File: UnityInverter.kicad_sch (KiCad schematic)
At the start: 5 parts, among them U9 LM358

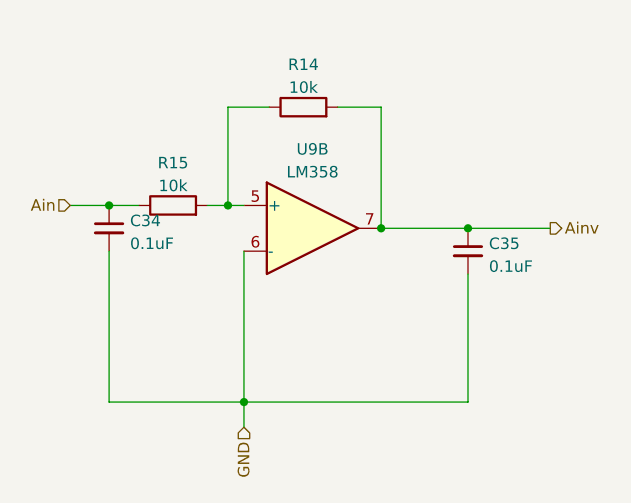
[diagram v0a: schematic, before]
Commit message: all SMD components going into boards
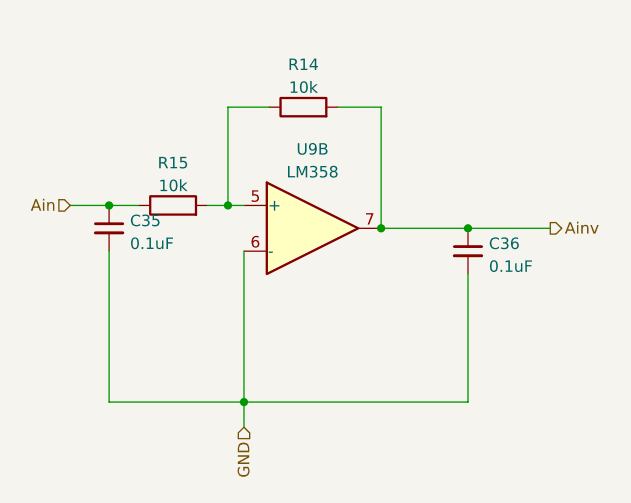
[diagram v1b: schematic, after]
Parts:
- U9: footprint (none) -> Package_TO_SOT_SMD:SOT-223-8
- renumbered C34 to C35, C35 to C36
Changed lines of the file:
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@@
   (symbol (lib_id "Device:C_Small") (at 112.776 105.156 0) (unit 1)
     (in_bom yes) (on_board yes) (fields_autoplaced)
-    (property "Reference" "C34" (id 0) (at 115.1001 104.3276 0)
+    (property "Reference" "C35" (id 0) (at 115.1001 104.3276 0)
       (effects (font (size 1.27 1.27)) (justify left))
     )
@@
     (property "Reference" "U9" (id 0) (at 135.382 96.3762 0))
     (property "Value" "LM358" (id 1) (at 135.382 98.9131 0))
-    (property "Footprint" "" (id 2) (at 135.382 105.156 0)
+    (property "Footprint" "Package_TO_SOT_SMD:SOT-223-8" (id 2) (at 135.382 105.156 0)
       (effects (font (size 1.27 1.27)) hide)
     )
@@
   (symbol (lib_id "Device:C_Small") (at 152.654 107.696 0) (unit 1)
     (in_bom yes) (on_board yes) (fields_autoplaced)
-    (property "Reference" "C35" (id 0) (at 154.9781 106.8676 0)
+    (property "Reference" "C36" (id 0) (at 154.9781 106.8676 0)
       (effects (font (size 1.27 1.27)) (justify left))
     )

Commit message: new board with SMD
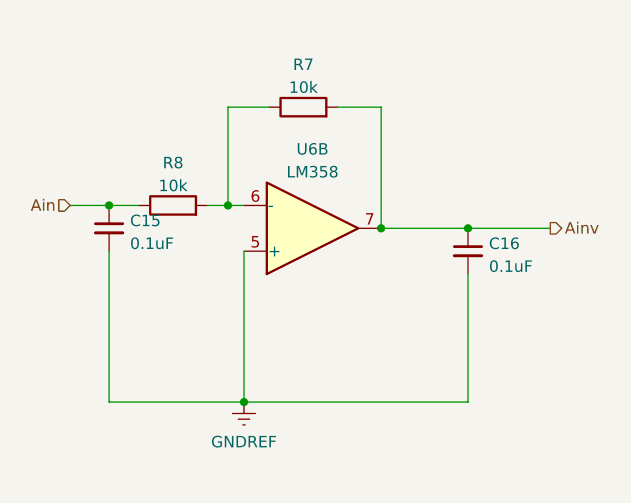
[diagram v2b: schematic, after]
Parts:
- renumbered C35 to C15, C36 to C16, R14 to R7, R15 to R8, U9 to U6
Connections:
- net at R7.1, R8.2: now also U6.6 (-); no longer U6.5 (+)
- net GND renamed GNDREF
- net GNDREF: now also U6.5 (+); no longer U6.6 (-)
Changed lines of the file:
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@@
-    (stroke (width 0) (type default) (color 0 0 0 0))
-  )
-  (wire (pts (xy 127.762 124.46) (xy 127.762 127.254))
     (stroke (width 0) (type default) (color 0 0 0 0))
   )
@@
     (effects (font (size 1.27 1.27)) (justify left))
   )
-  (hierarchical_label "GND" (shape input) (at 127.762 127.254 270)
-    (effects (font (size 1.27 1.27)) (justify right))
-  )
   (symbol (lib_id "Device:C_Small") (at 112.776 105.156 0) (unit 1)
     (in_bom yes) (on_board yes) (fields_autoplaced)
-    (property "Reference" "C35" (id 0) (at 115.1001 104.3276 0)
+    (property "Reference" "C15" (id 0) (at 115.1001 104.3276 0)
       (effects (font (size 1.27 1.27)) (justify left))
     )
@@
     (pin "2")
   )
-  (symbol (lib_id "Amplifier_Operational:LM358") (at 135.382 105.156 0) (unit 2)
+  (symbol (lib_id "Amplifier_Operational:LM358") (at 135.382 105.156 0) (mirror x) (unit 2)
     (in_bom yes) (on_board yes) (fields_autoplaced)
-    (property "Reference" "U9" (id 0) (at 135.382 96.3762 0))
+    (property "Reference" "U6" (id 0) (at 135.382 96.3762 0))
     (property "Value" "LM358" (id 1) (at 135.382 98.9131 0))
     (property "Footprint" "Package_TO_SOT_SMD:SOT-223-8" (id 2) (at 135.382 105.156 0)
@@
   (symbol (lib_id "Device:C_Small") (at 152.654 107.696 0) (unit 1)
     (in_bom yes) (on_board yes) (fields_autoplaced)
-    (property "Reference" "C36" (id 0) (at 154.9781 106.8676 0)
+    (property "Reference" "C16" (id 0) (at 154.9781 106.8676 0)
       (effects (font (size 1.27 1.27)) (justify left))
     )
@@
   (symbol (lib_id "Device:R") (at 119.888 102.616 90) (unit 1)
     (in_bom yes) (on_board yes) (fields_autoplaced)
-    (property "Reference" "R15" (id 0) (at 119.888 97.9002 90))
+    (property "Reference" "R8" (id 0) (at 119.888 97.9002 90))
     (property "Value" "10k" (id 1) (at 119.888 100.4371 90))
     (property "Footprint" "Resistor_SMD:R_0603_1608Metric" (id 2) (at 119.888 104.394 90)
@@
   (symbol (lib_id "Device:R") (at 134.366 91.694 90) (unit 1)
     (in_bom yes) (on_board yes) (fields_autoplaced)
-    (property "Reference" "R14" (id 0) (at 134.366 86.9782 90))
+    (property "Reference" "R7" (id 0) (at 134.366 86.9782 90))
     (property "Value" "10k" (id 1) (at 134.366 89.5151 90))
     (property "Footprint" "Resistor_SMD:R_0603_1608Metric" (id 2) (at 134.366 93.472 90)
@@
     (pin "2")
   )
+  (symbol (lib_id "power:GNDREF") (at 127.762 124.46 0) (unit 1)
+    (in_bom yes) (on_board yes) (fields_autoplaced)
+    (property "Reference" "#PWR017" (id 0) (at 127.762 130.81 0)
+      (effects (font (size 1.27 1.27)) hide)
+    )
+    (property "Value" "GNDREF" (id 1) (at 127.762 128.9034 0))
+    (property "Footprint" "" (id 2) (at 127.762 124.46 0)
+      (effects (font (size 1.27 1.27)) hide)
+    )
+    (property "Datasheet" "" (id 3) (at 127.762 124.46 0)
+      (effects (font (size 1.27 1.27)) hide)
+    )
+    (pin "1")
+  )
 )

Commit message: New single board with all SMD in progress
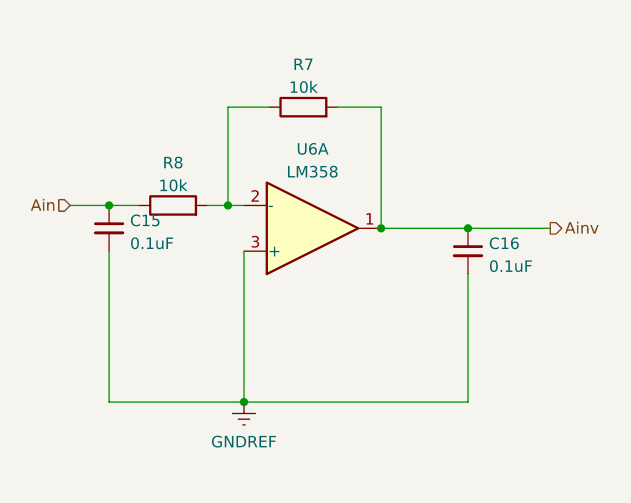
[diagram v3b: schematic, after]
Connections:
- net Ainv: now also U6.1; no longer U6.7
- net GNDREF: now also U6.3 (+); no longer U6.5 (+)
- net at R7.1, R8.2: now also U6.2 (-); no longer U6.6 (-)
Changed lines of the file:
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@@
     (pin "2")
   )
-  (symbol (lib_id "Amplifier_Operational:LM358") (at 135.382 105.156 0) (mirror x) (unit 2)
+  (symbol (lib_id "Amplifier_Operational:LM358") (at 135.382 105.156 0) (mirror x) (unit 1)
     (in_bom yes) (on_board yes) (fields_autoplaced)
     (property "Reference" "U6" (id 0) (at 135.382 96.3762 0))

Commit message: Updated improved board for all SMD
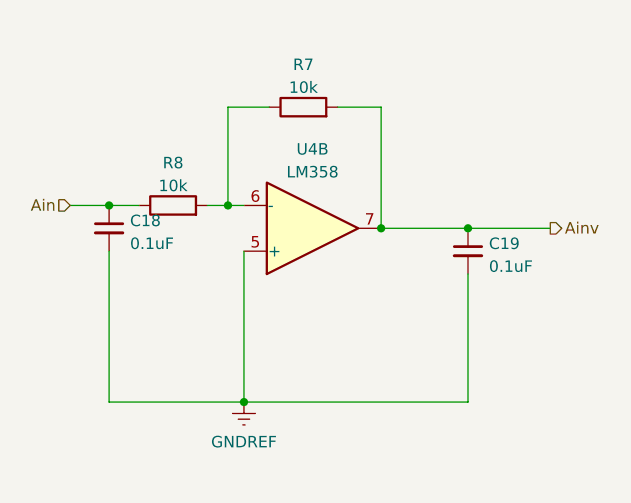
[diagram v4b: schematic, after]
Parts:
- renumbered C15 to C18, C16 to C19, U6 to U4
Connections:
- net Ainv: now also U4.7; no longer U4.1
- net GNDREF: now also U4.5 (+); no longer U4.3 (+)
- net at R7.1, R8.2: now also U4.6 (-); no longer U4.2 (-)
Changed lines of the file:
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@@
   (symbol (lib_id "Device:C_Small") (at 112.776 105.156 0) (unit 1)
     (in_bom yes) (on_board yes) (fields_autoplaced)
-    (property "Reference" "C15" (id 0) (at 115.1001 104.3276 0)
+    (property "Reference" "C18" (id 0) (at 115.1001 104.3276 0)
       (effects (font (size 1.27 1.27)) (justify left))
     )
@@
     (pin "2")
   )
-  (symbol (lib_id "Amplifier_Operational:LM358") (at 135.382 105.156 0) (mirror x) (unit 1)
+  (symbol (lib_id "Amplifier_Operational:LM358") (at 135.382 105.156 0) (mirror x) (unit 2)
     (in_bom yes) (on_board yes) (fields_autoplaced)
-    (property "Reference" "U6" (id 0) (at 135.382 96.3762 0))
+    (property "Reference" "U4" (id 0) (at 135.382 96.3762 0))
     (property "Value" "LM358" (id 1) (at 135.382 98.9131 0))
     (property "Footprint" "Package_TO_SOT_SMD:SOT-223-8" (id 2) (at 135.382 105.156 0)
@@
   (symbol (lib_id "Device:C_Small") (at 152.654 107.696 0) (unit 1)
     (in_bom yes) (on_board yes) (fields_autoplaced)
-    (property "Reference" "C16" (id 0) (at 154.9781 106.8676 0)
+    (property "Reference" "C19" (id 0) (at 154.9781 106.8676 0)
       (effects (font (size 1.27 1.27)) (justify left))
     )
@@
   (symbol (lib_id "power:GNDREF") (at 127.762 124.46 0) (unit 1)
     (in_bom yes) (on_board yes) (fields_autoplaced)
-    (property "Reference" "#PWR017" (id 0) (at 127.762 130.81 0)
+    (property "Reference" "#PWR020" (id 0) (at 127.762 130.81 0)
       (effects (font (size 1.27 1.27)) hide)
     )

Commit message: added new op amps and used automated traces due to complexity
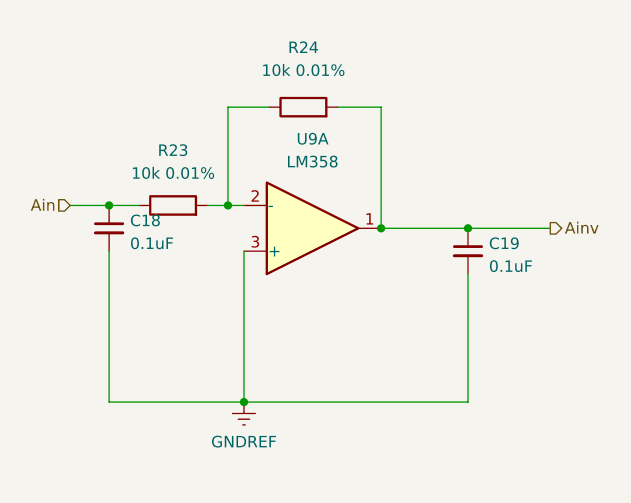
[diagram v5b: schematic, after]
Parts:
- R23: renamed from R8; value 10k -> 10k 0.01%
- R24: renamed from R7; value 10k -> 10k 0.01%
- U9: renamed from U4; footprint Package_TO_SOT_SMD:SOT-223-8 -> Package_SO:TSSOP-8_4.4x3mm_P0.65mm
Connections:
- net Ainv: now also U9.1; no longer U9.7
- net GNDREF: now also U9.3 (+); no longer U9.5 (+)
- net at R23.2, R24.1: now also U9.2 (-); no longer U9.6 (-)
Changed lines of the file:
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@@
     (pin "2")
   )
-  (symbol (lib_id "Amplifier_Operational:LM358") (at 135.382 105.156 0) (mirror x) (unit 2)
+  (symbol (lib_id "Amplifier_Operational:LM358") (at 135.382 105.156 0) (mirror x) (unit 1)
     (in_bom yes) (on_board yes) (fields_autoplaced)
-    (property "Reference" "U4" (id 0) (at 135.382 96.3762 0))
-    (property "Value" "LM358" (id 1) (at 135.382 98.9131 0))
-    (property "Footprint" "Package_TO_SOT_SMD:SOT-223-8" (id 2) (at 135.382 105.156 0)
+    (property "Reference" "U9" (id 0) (at 135.382 95.25 0))
+    (property "Value" "LM358" (id 1) (at 135.382 97.79 0))
+    (property "Footprint" "Package_SO:TSSOP-8_4.4x3mm_P0.65mm" (id 2) (at 135.382 105.156 0)
       (effects (font (size 1.27 1.27)) hide)
     )
@@
   (symbol (lib_id "Device:R") (at 119.888 102.616 90) (unit 1)
     (in_bom yes) (on_board yes) (fields_autoplaced)
-    (property "Reference" "R8" (id 0) (at 119.888 97.9002 90))
-    (property "Value" "10k" (id 1) (at 119.888 100.4371 90))
+    (property "Reference" "R23" (id 0) (at 119.888 96.52 90))
+    (property "Value" "10k 0.01%" (id 1) (at 119.888 99.06 90))
     (property "Footprint" "Resistor_SMD:R_0603_1608Metric" (id 2) (at 119.888 104.394 90)
       (effects (font (size 1.27 1.27)) hide)
@@
   (symbol (lib_id "Device:R") (at 134.366 91.694 90) (unit 1)
     (in_bom yes) (on_board yes) (fields_autoplaced)
-    (property "Reference" "R7" (id 0) (at 134.366 86.9782 90))
-    (property "Value" "10k" (id 1) (at 134.366 89.5151 90))
+    (property "Reference" "R24" (id 0) (at 134.366 85.09 90))
+    (property "Value" "10k 0.01%" (id 1) (at 134.366 87.63 90))
     (property "Footprint" "Resistor_SMD:R_0603_1608Metric" (id 2) (at 134.366 93.472 90)
       (effects (font (size 1.27 1.27)) hide)

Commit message: new EMC-EMI layout with improved suppression
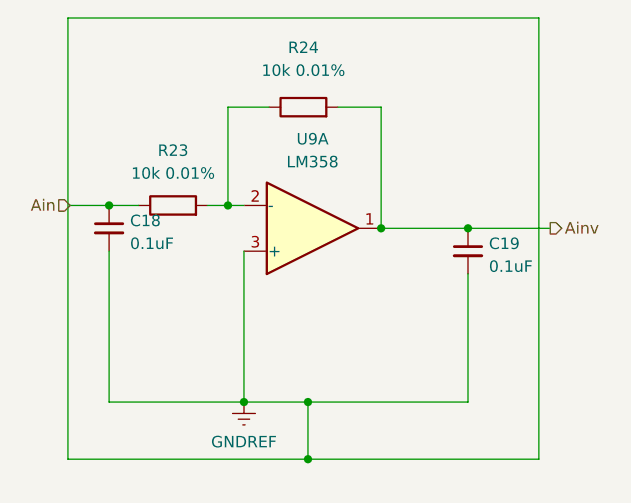
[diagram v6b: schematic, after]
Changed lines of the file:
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@@
   (junction (at 152.654 105.156) (diameter 0) (color 0 0 0 0)
   )
+  (junction (at 134.874 124.46) (diameter 0) (color 0 0 0 0)
+  )
   (junction (at 112.776 102.616) (diameter 0) (color 0 0 0 0)
+  )
+  (junction (at 134.874 130.81) (diameter 0) (color 0 0 0 0)
   )
   (junction (at 143.002 105.156) (diameter 0) (color 0 0 0 0)
@@
     (stroke (width 0) (type default) (color 0 0 0 0))
   )
+  (wire (pts (xy 134.874 130.81) (xy 160.528 130.81))
+    (stroke (width 0) (type default) (color 0 0 0 0))
+  )
   (wire (pts (xy 125.984 91.694) (xy 125.984 102.616))
     (stroke (width 0) (type default) (color 0 0 0 0))
   )
-  (wire (pts (xy 127.762 124.46) (xy 152.654 124.46))
+  (wire (pts (xy 127.762 124.46) (xy 134.874 124.46))
     (stroke (width 0) (type default) (color 0 0 0 0))
   )
   (wire (pts (xy 138.176 91.694) (xy 143.002 91.694))
+    (stroke (width 0) (type default) (color 0 0 0 0))
+  )
+  (wire (pts (xy 160.528 81.788) (xy 160.528 130.81))
     (stroke (width 0) (type default) (color 0 0 0 0))
   )
@@
     (stroke (width 0) (type default) (color 0 0 0 0))
   )
+  (wire (pts (xy 108.204 130.81) (xy 134.874 130.81))
+    (stroke (width 0) (type default) (color 0 0 0 0))
+  )
   (wire (pts (xy 143.002 105.156) (xy 152.654 105.156))
     (stroke (width 0) (type default) (color 0 0 0 0))
@@
     (stroke (width 0) (type default) (color 0 0 0 0))
   )
+  (wire (pts (xy 134.874 130.81) (xy 134.874 124.46))
+    (stroke (width 0) (type default) (color 0 0 0 0))
+  )
+  (wire (pts (xy 108.204 81.788) (xy 160.528 81.788))
+    (stroke (width 0) (type default) (color 0 0 0 0))
+  )
   (wire (pts (xy 112.776 124.46) (xy 127.762 124.46))
+    (stroke (width 0) (type default) (color 0 0 0 0))
+  )
+  (wire (pts (xy 134.874 124.46) (xy 152.654 124.46))
     (stroke (width 0) (type default) (color 0 0 0 0))
   )
@@
     (stroke (width 0) (type default) (color 0 0 0 0))
   )
+  (wire (pts (xy 108.204 130.81) (xy 108.204 81.788))
+    (stroke (width 0) (type default) (color 0 0 0 0))
+  )
